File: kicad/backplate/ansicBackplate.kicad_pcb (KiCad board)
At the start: 2 copper layers, 123 x 102.5 mm, 0 parts

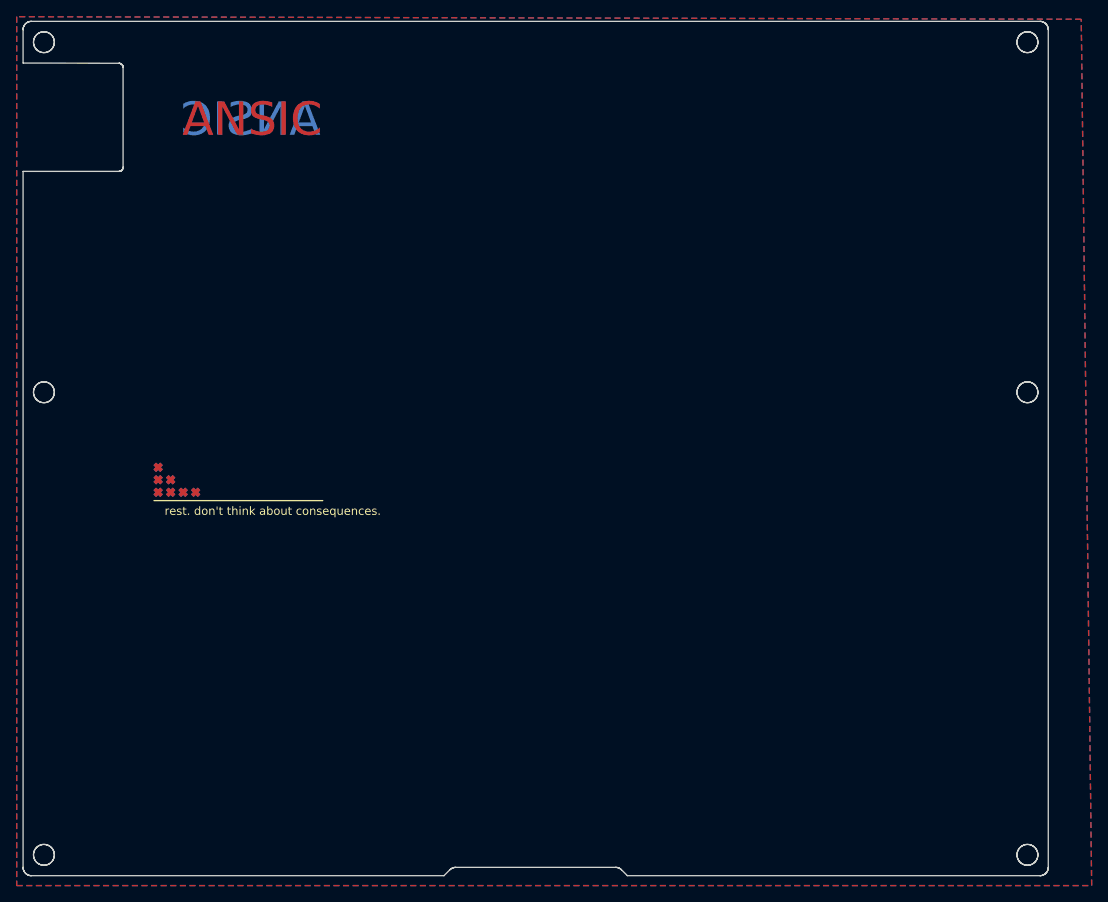
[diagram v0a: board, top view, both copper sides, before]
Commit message: made bumpon place on backplate
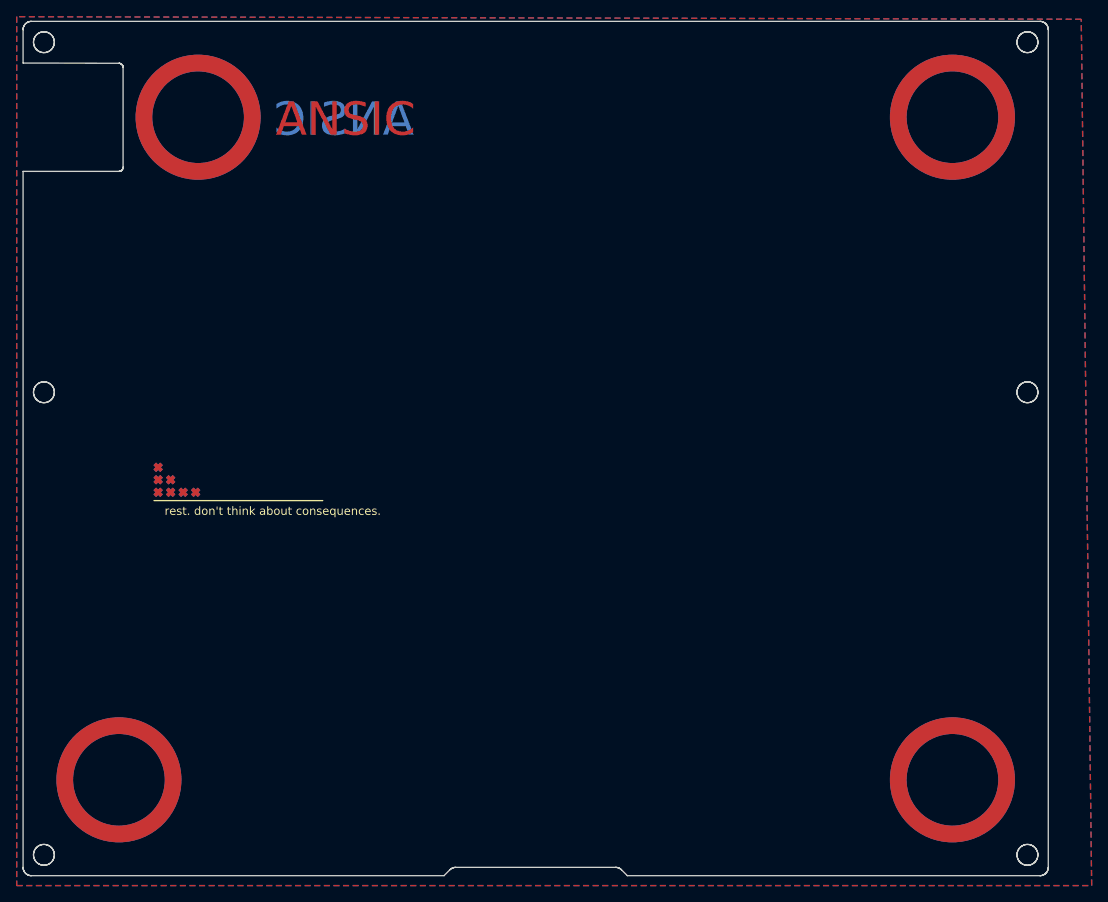
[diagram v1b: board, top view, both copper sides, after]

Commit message: add bumpon and drain footprint
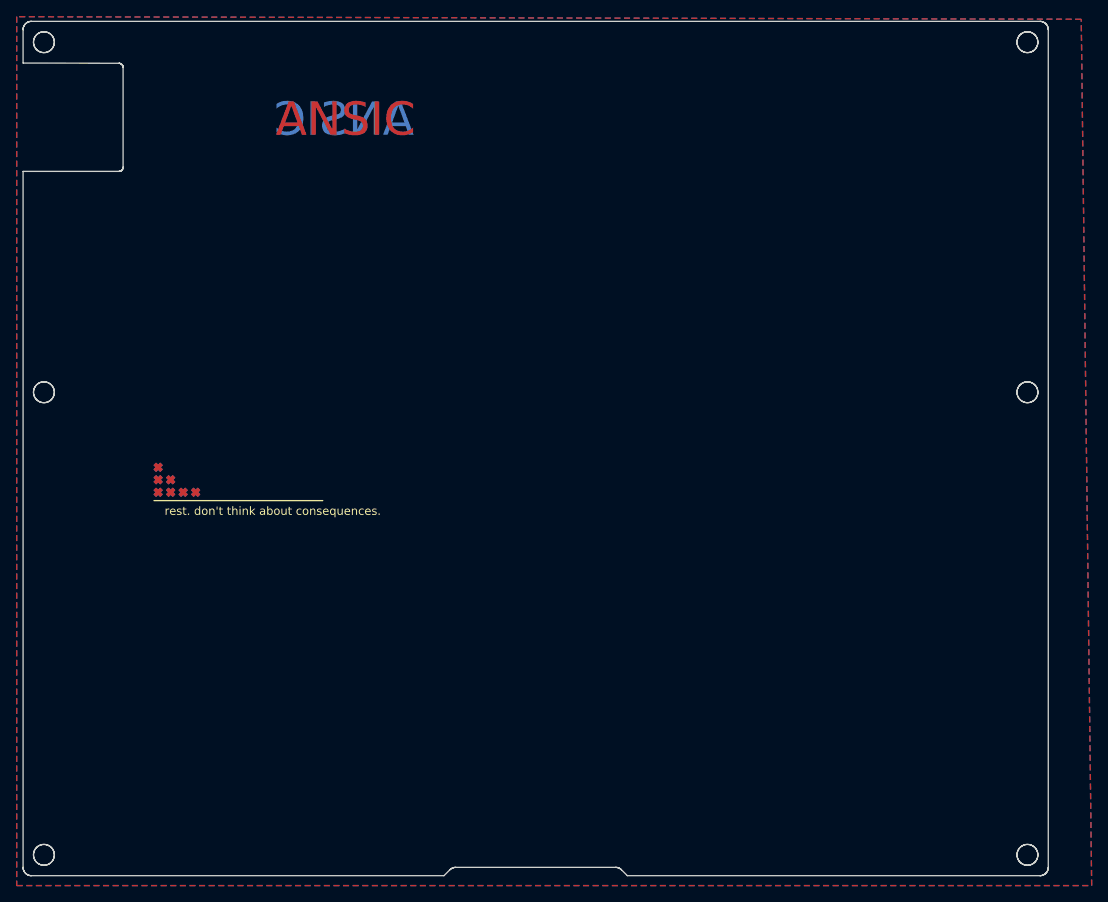
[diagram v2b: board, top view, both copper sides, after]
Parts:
- added REF**: Backplate-BumponGuide-11mm, ansic-CustomFoot:Backplate-BumponGuide-11mm, F.Cu at (169.0, 36.5)
- added REF**: Backplate-BumponGuide-11mm, ansic-CustomFoot:Backplate-BumponGuide-11mm, F.Cu at (78.5, 36.5)
- added REF**: Backplate-BumponGuide-11mm, ansic-CustomFoot:Backplate-BumponGuide-11mm, F.Cu at (169.0, 116.0)
- added REF**: Backplate-BumponGuide-11mm, ansic-CustomFoot:Backplate-BumponGuide-11mm, F.Cu at (69.0, 116.0)
